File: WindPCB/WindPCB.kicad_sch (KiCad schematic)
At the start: 24 parts, among them J1 1267, J2 1267, J3 1267, J4 1267, J5 1267, J6 Conn_01x04, U1 LM7808_TO220, U3 LM7805_TO220, U4 MCP2562-E-P, U5 ESP32-C3_SUPERMINI

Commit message: Lot of good stuff
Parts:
- removed C1: 0.1, Capacitor_THT:C_Disc_D6.0mm_W2.5mm_P5.00mm, symbol Device:C
- removed R1: 2200, Resistor_THT:R_Axial_DIN0204_L3.6mm_D1.6mm_P7.62mm_Horizontal, symbol Device:R
- removed RV1: R_Potentiometer_Small, Potentiometer_THT:Potentiometer_Bourns_3296W_Vertical, symbol Device:R_Potentiometer_Small
- removed U3: LM7805_TO220, Package_TO_SOT_THT:TO-220-3_Vertical, symbol Regulator_Linear:LM7805_TO220
- removed U5: ESP32-C3_SUPERMINI, Library:WAVESHARE_DEVKIT_ESP32-C3-ZERO, symbol Espressif:ESP32-C3_SUPERMINI
- added C5: 100nF, Capacitor_THT:C_Disc_D6.0mm_W2.5mm_P5.00mm, symbol Device:C
- added C6: 330nF, Capacitor_THT:C_Disc_D6.0mm_W2.5mm_P5.00mm, symbol Device:C
- added C7: 1nF, Capacitor_THT:C_Disc_D6.0mm_W2.5mm_P5.00mm, symbol Device:C
- added D2: LED, LED_THT:LED_D3.0mm, symbol Device:LED
- added JP2: Jumper_2_Open, Connector_PinHeader_2.54mm:PinHeader_1x02_P2.54mm_Vertical, symbol Jumper:Jumper_2_Open
- added JP3: Jumper_3_Bridged12, Connector_PinHeader_2.54mm:PinHeader_1x03_P2.54mm_Vertical, symbol Jumper:Jumper_3_Bridged12
- added R11: 100, Resistor_THT:R_Axial_DIN0204_L3.6mm_D1.6mm_P7.62mm_Horizontal, symbol Device:R
- added R12: 3K3, Resistor_THT:R_Axial_DIN0204_L3.6mm_D1.6mm_P7.62mm_Horizontal, symbol Device:R
- added R5: 2K2, Resistor_THT:R_Axial_DIN0204_L3.6mm_D1.6mm_P7.62mm_Horizontal, symbol Device:R
- added U2: TSR_1-2450, Converter_DCDC:Converter_DCDC_TRACO_TSR-1_THT, symbol Regulator_Switching:TSR_1-2450
- added U3: SeeeduinoXIAO, Seeeduino:Seeeduino XIAO-MOUDLE14P-2.54-21X17.8MM_1, symbol Seeduino:SeeeduinoXIAO
- C2: value 0.1 -> 100nF
- C3: value 0.1 -> 0.1uF
- C4: value 0.1 -> 1nF
- J_COS1: renamed from J3; value 1267 -> COS; footprint Library:KEYSTONE_1267 -> Custom:KEYSTONE_1267
- J_GND1: renamed from J4; value 1267 -> GND; footprint Library:KEYSTONE_1267 -> Custom:KEYSTONE_1267
- J_SIN1: renamed from J2; value 1267 -> SIN; footprint Library:KEYSTONE_1267 -> Custom:KEYSTONE_1267
- J_SPEED1: renamed from J1; value 1267 -> SPEED; footprint Library:KEYSTONE_1267 -> Custom:KEYSTONE_1267
- J_VCC1: renamed from J5; value 1267 -> VCC; footprint Library:KEYSTONE_1267 -> Custom:KEYSTONE_1267
- R2, R3: value 2200 -> 1000
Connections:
- net +12V: now also C6.1, U2.3 (Vout)
- net +3.3V: now also U3.12 (3V3)
- net +5V: now also JP2.2 (B), JP3.3 (B), R5.1, U3.14 (5V), U3.15 (5V); no longer C4.2
- net +8V: now also C5.2, JP3.1 (A); no longer C2.2, J_VCC1.1
- net GND: now also C4.2, R2.2, R3.2, C5.1, C6.2, C7.2, R11.2, R12.2, U2.2 (GND), U3.13 (GND), U3.16 (GND), U3.20 (GND); no longer C4.1, RV2.3, RV3.3
- net at J6.2 (Pin_2), U4.7 (CANH): now also JP1.2 (B); no longer R7.1
- net at D1.1 (K): now also U3.10 (PA5_A9_D9_MISO)
- net at RV2.1: now also J_SIN1.1; no longer R2.2
- net at RV2.2: now also C7.1, U3.5 (PA8_A4_D4_SDA)
- net at R2.1: now also RV2.3; no longer J_SIN1.1
- net at J6.1 (Pin_1), U4.6 (CANL): now also R7.1; no longer JP1.2 (B)
- net at J_SPEED1.1: now also R12.1, R5.2, U3.11 (PA6_A10_D10_MOSI)
- net at R3.1: now also RV3.3; no longer J_COS1.1
- net at RV3.1: now also J_COS1.1; no longer R3.2
- net at RV3.2: now also C4.1, U3.6 (PA9_A5_D5_SCL)
- net at U4.4 (RXD): now also U3.7 (PB08_A6_D6_TX)
- net at U4.1 (TXD): now also U3.8 (PB09_A7_D7_RX)
- new net: C2.2, JP2.1 (A), U2.1 (Vin)
- new net: D2.1 (K), U3.9 (PA7_A8_D8_SCK)
- new net: D2.2 (A), R11.1
- new net: JP3.2 (C), J_VCC1.1
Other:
- moved on the sheet: C2, C3, D1, J6, JP1, J_COS1, J_GND1, J_SIN1, J_SPEED1, J_VCC1, R2, R3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

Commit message: Changed analog pins
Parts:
- R2, R3: value 1000 -> 2K
- RV2, RV3: value R_Potentiometer_Small -> 5K
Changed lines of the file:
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@@
 			)
 		)
-		(property "Value" "R_Potentiometer_Small"
-			(at 120.142 86.614 0)
+		(property "Value" "5K"
+			(at 139.7 78.486 0)
 			(effects
 				(font
@@
 				)
 				(justify right)
-				(hide yes)
 			)
 		)
@@
 			)
 		)
-		(property "Value" "1000"
+		(property "Value" "2K"
 			(at 139.7 87.6299 0)
 			(effects
@@
 			)
 		)
-		(property "Value" "1000"
+		(property "Value" "2K"
 			(at 148.59 88.8999 0)
 			(effects
@@
 			)
 		)
-		(property "Value" "R_Potentiometer_Small"
-			(at 129.032 90.424 0)
+		(property "Value" "5K"
+			(at 148.59 82.296 0)
 			(effects
 				(font
@@
 				)
 				(justify right)
-				(hide yes)
-			)
-		)
+			)
+		)

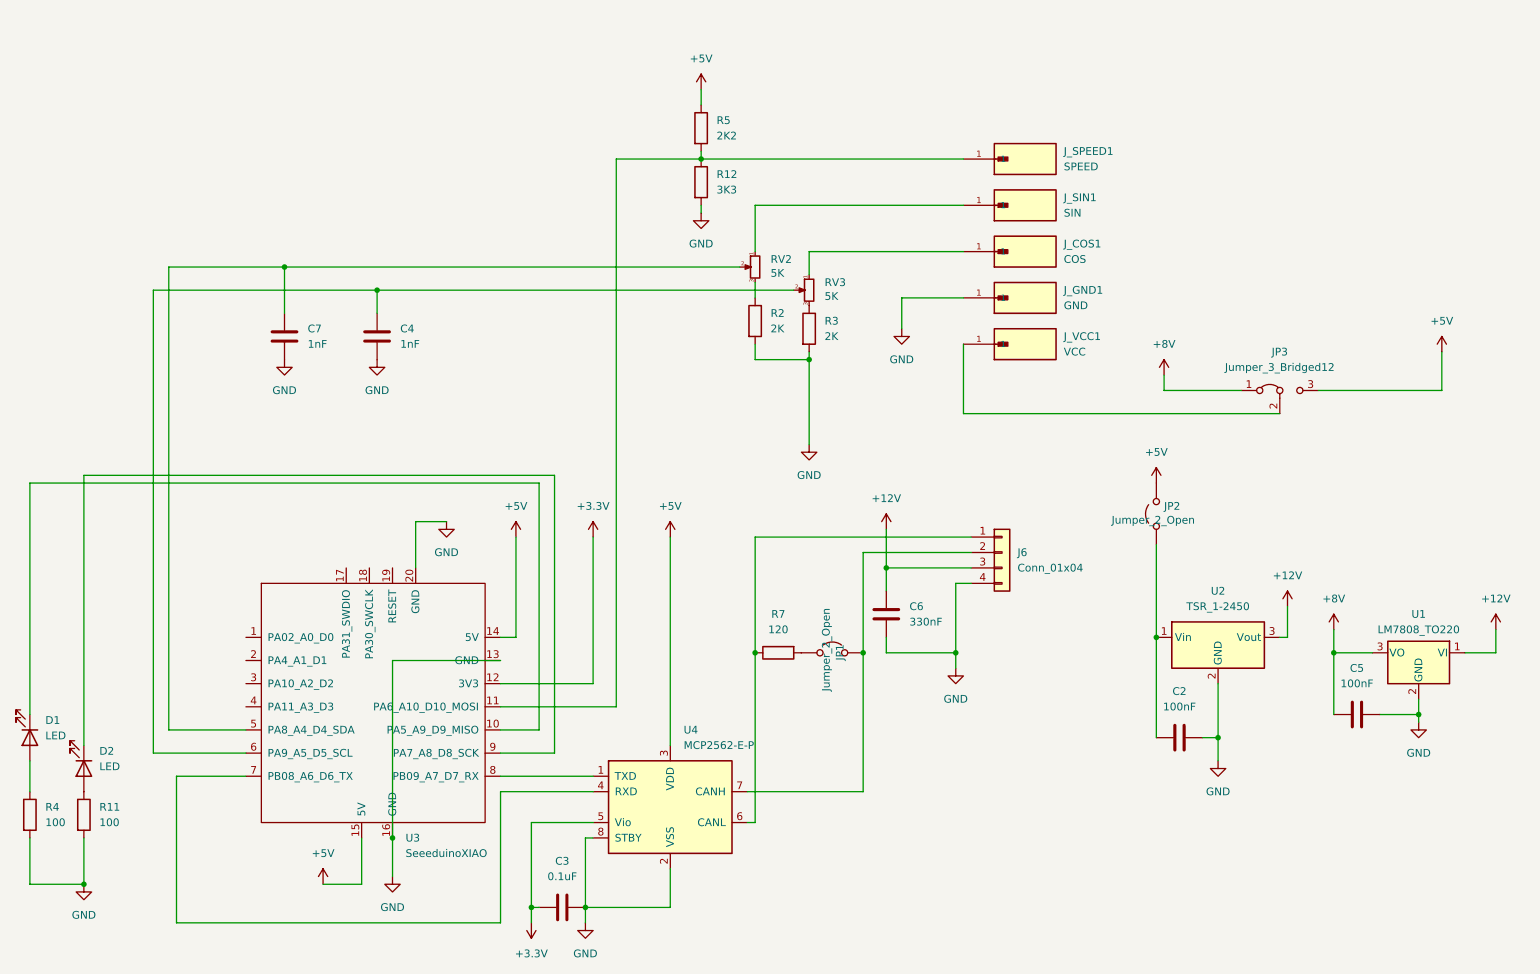
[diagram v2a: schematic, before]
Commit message: Vane type is now configurable at runtime and part of the configuration. The code to apply a calibration is now centralized (the CommandHandler "borrows" the callback function from the AutoCalibration class). Experiments on buffering sin/cos values (buffering is better...). Experimental ADS1115. New PCB: now 12V can be excluded so to operate with both N2K power and USB (at teh same time).
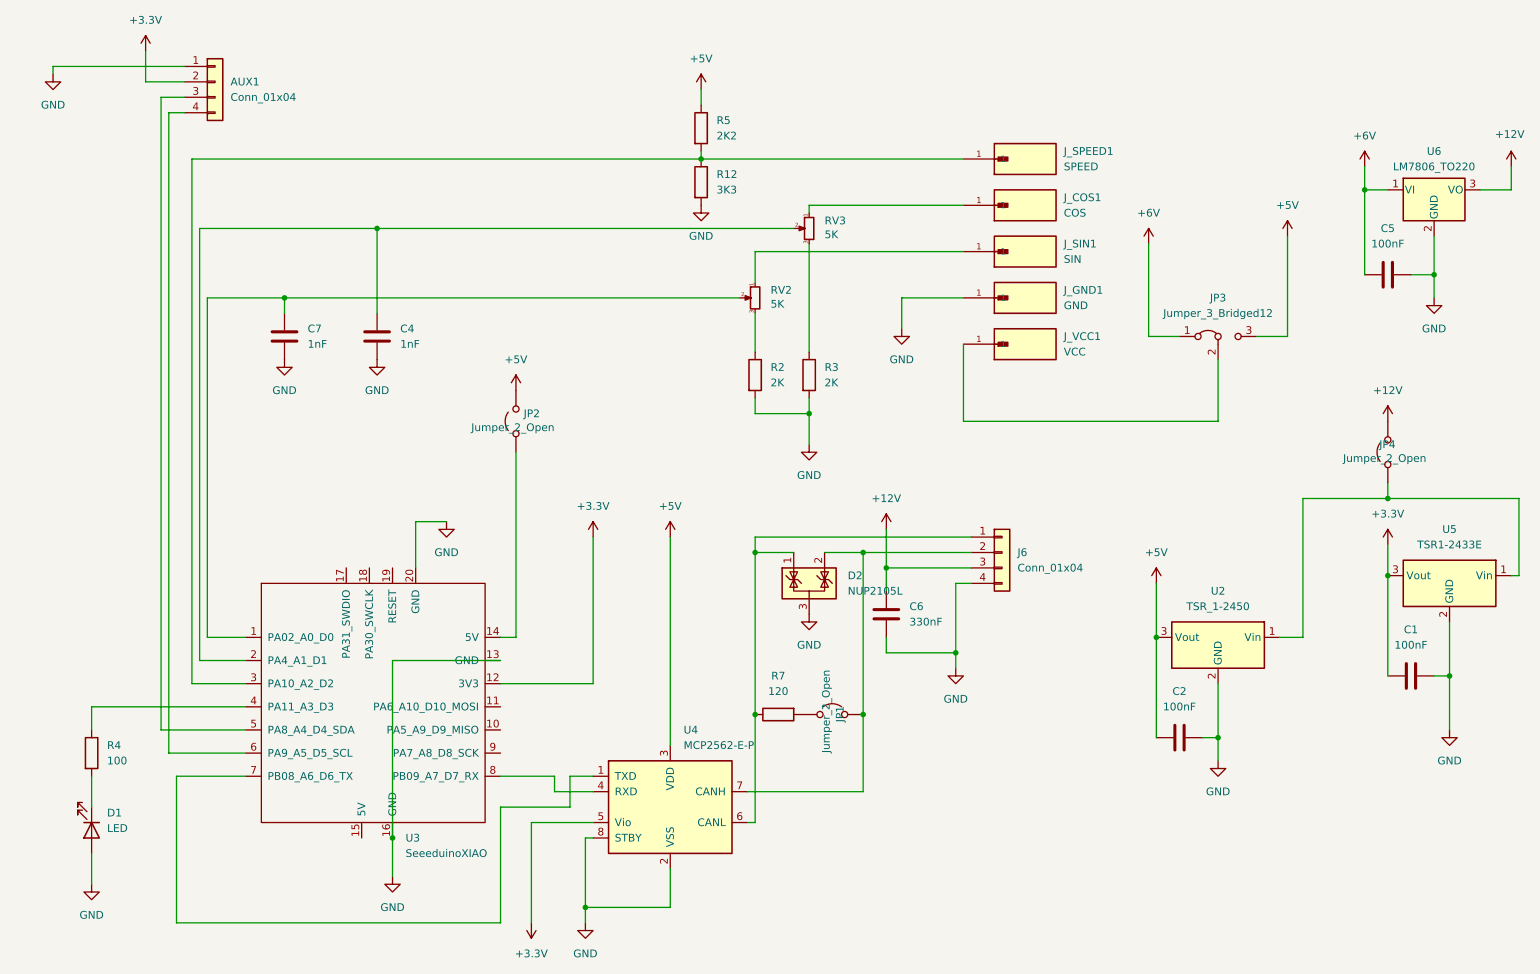
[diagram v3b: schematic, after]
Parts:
- removed C3: 0.1uF, Capacitor_THT:C_Disc_D6.0mm_W2.5mm_P5.00mm, symbol Device:C
- removed D2: LED, LED_THT:LED_D3.0mm, symbol Device:LED
- removed R11: 100, Resistor_THT:R_Axial_DIN0204_L3.6mm_D1.6mm_P7.62mm_Horizontal, symbol Device:R
- removed U1: LM7808_TO220, Package_TO_SOT_THT:TO-220-3_Vertical, symbol Regulator_Linear:LM7808_TO220
- added AUX1: Conn_01x04, Connector_JST:JST_EH_B4B-EH-A_1x04_P2.50mm_Vertical, symbol Connector_Generic:Conn_01x04
- added C1: 100nF, Capacitor_THT:C_Disc_D6.0mm_W2.5mm_P5.00mm, symbol Device:C
- added D2: NUP2105L, Package_TO_SOT_SMD:SOT-23, symbol Power_Protection:NUP2105L
- added JP4: Jumper_2_Open, Connector_PinHeader_2.54mm:PinHeader_1x02_P2.54mm_Vertical, symbol Jumper:Jumper_2_Open
- added U5: TSR1-2433E, Converter_DCDC:Converter_DCDC_TRACO_TSR-1_THT, symbol Regulator_Switching:TSR1-2433E
- added U6: LM7806_TO220, Package_TO_SOT_THT:TO-220-3_Vertical, symbol Regulator_Linear:LM7806_TO220
- J_COS1, J_GND1, J_SIN1, J_SPEED1, J_VCC1: footprint Custom:KEYSTONE_1267 -> connectors:KEYSTONE_1267
- U3: footprint Seeeduino:Seeeduino XIAO-MOUDLE14P-2.54-21X17.8MM_1 -> seeduino:Seeeduino XIAO-MOUDLE14P-2.54-21X17.8MM_1
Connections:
- net +12V: now also JP4.2 (B), U6.3 (VO); no longer U2.3 (Vout)
- net +3.3V: now also AUX1.2 (Pin_2), C1.2, U5.3 (Vout)
- net +5V: now also C2.2, U2.3 (Vout); no longer U3.14 (5V), U3.15 (5V)
- net GND: now also D1.2 (A), AUX1.1 (Pin_1), C1.1, D2.3 (A), U5.2 (GND), U6.2 (GND); no longer R4.2
- net at R4.1: now also U3.4 (PA11_A3_D3); no longer D1.2 (A)
- net at J6.1 (Pin_1), R7.1, U4.6 (CANL): now also D2.1 (K)
- net at U3.1 (PA02_A0_D0): now also C7.1, RV2.2
- net at D1.1 (K): now also R4.2; no longer U3.10 (PA5_A9_D9_MISO)
- net at J_SPEED1.1, R12.1, R5.2: now also U3.3 (PA10_A2_D2); no longer U3.11 (PA6_A10_D10_MOSI)
- net at U3.2 (PA4_A1_D1): now also C4.1, RV3.2
- net at U3.7 (PB08_A6_D6_TX): now also U4.1 (TXD); no longer U4.4 (RXD)
- net at U3.8 (PB09_A7_D7_RX): now also U4.4 (RXD); no longer U4.1 (TXD)
- net at J6.2 (Pin_2), JP1.2 (B), U4.7 (CANH): now also D2.2 (K)
- net +8V renamed +6V
- net +6V: now also U6.1 (VI)
- new net: JP2.1 (A), U3.14 (5V)
- new net: AUX1.3 (Pin_3), U3.5 (PA8_A4_D4_SDA)
- new net: AUX1.4 (Pin_4), U3.6 (PA9_A5_D5_SCL)
- new net: JP4.1 (A), U2.1 (Vin), U5.1 (Vin)
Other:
- moved on the sheet: C5, D1, JP1, JP2, JP3, J_COS1, J_SIN1, R2, R3, R4, R7, RV2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

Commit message: Removed not used code. Dropeed ADS1115 (not advantages). Added suppoer to change teh device name (BLE). Moved N2K info to Constants. Other minor changes and improvements.
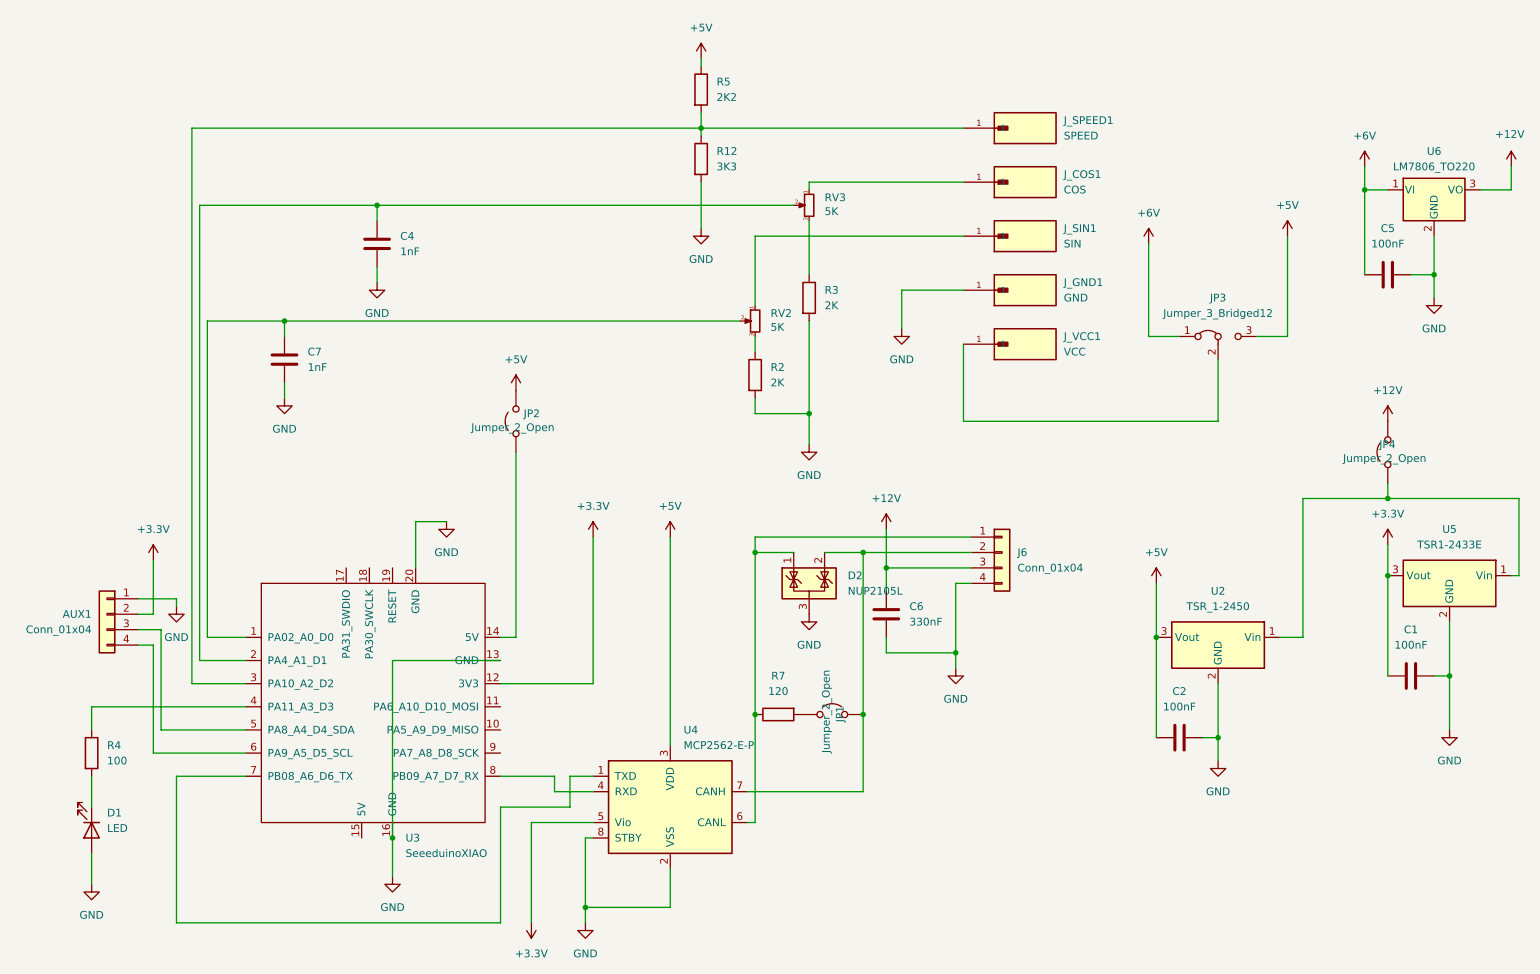
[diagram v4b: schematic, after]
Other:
- moved on the sheet: AUX1, C4, C7, J_COS1, J_GND1, J_SIN1, J_SPEED1, R12, R3, R5, RV2, RV3
